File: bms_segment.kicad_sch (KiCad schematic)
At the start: 100 parts, among them J1 Conn_01x04, J2 Conn_01x04, J3 Conn_01x06, J4 Conn_01x13, SW1 SW_Push, U1 LMR516xx, U2 MAX14921, U3 ADuM1252, U4 STM32F103C8Tx, U5 MAX11163, U6 REF61xx

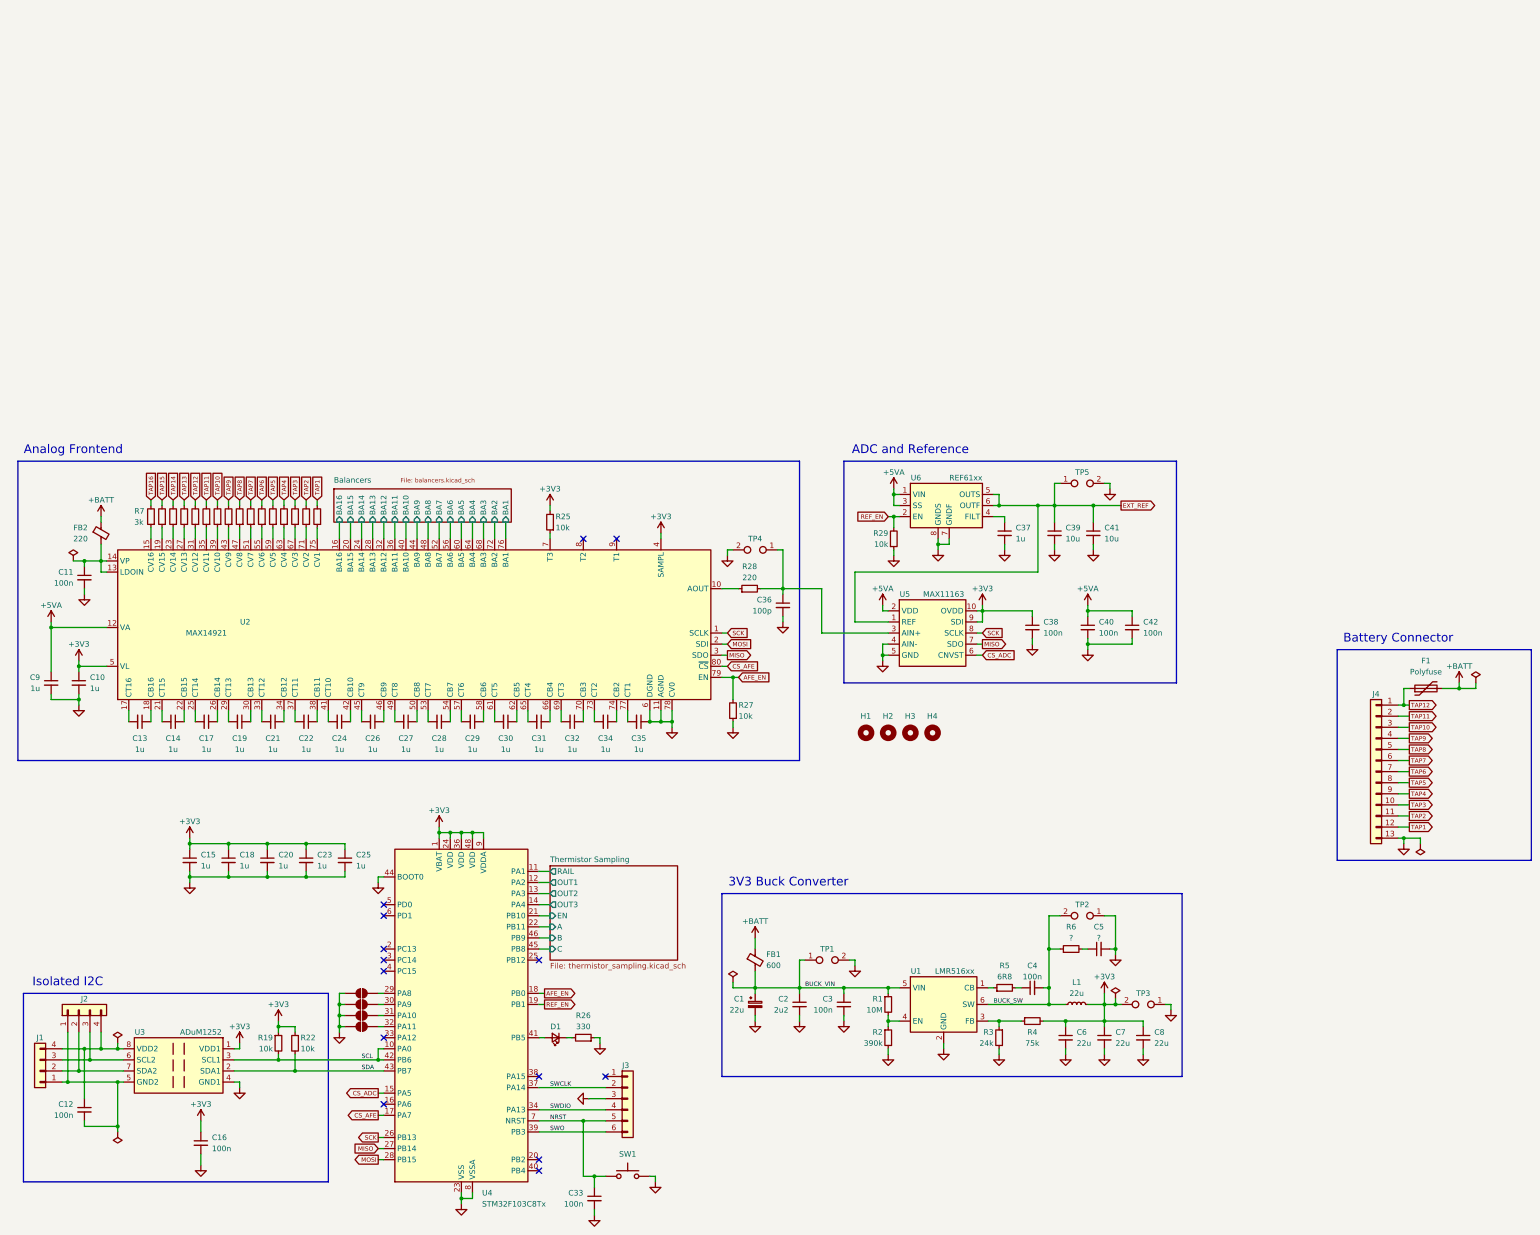
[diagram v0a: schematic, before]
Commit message: schematic: Add board interconnect connectors
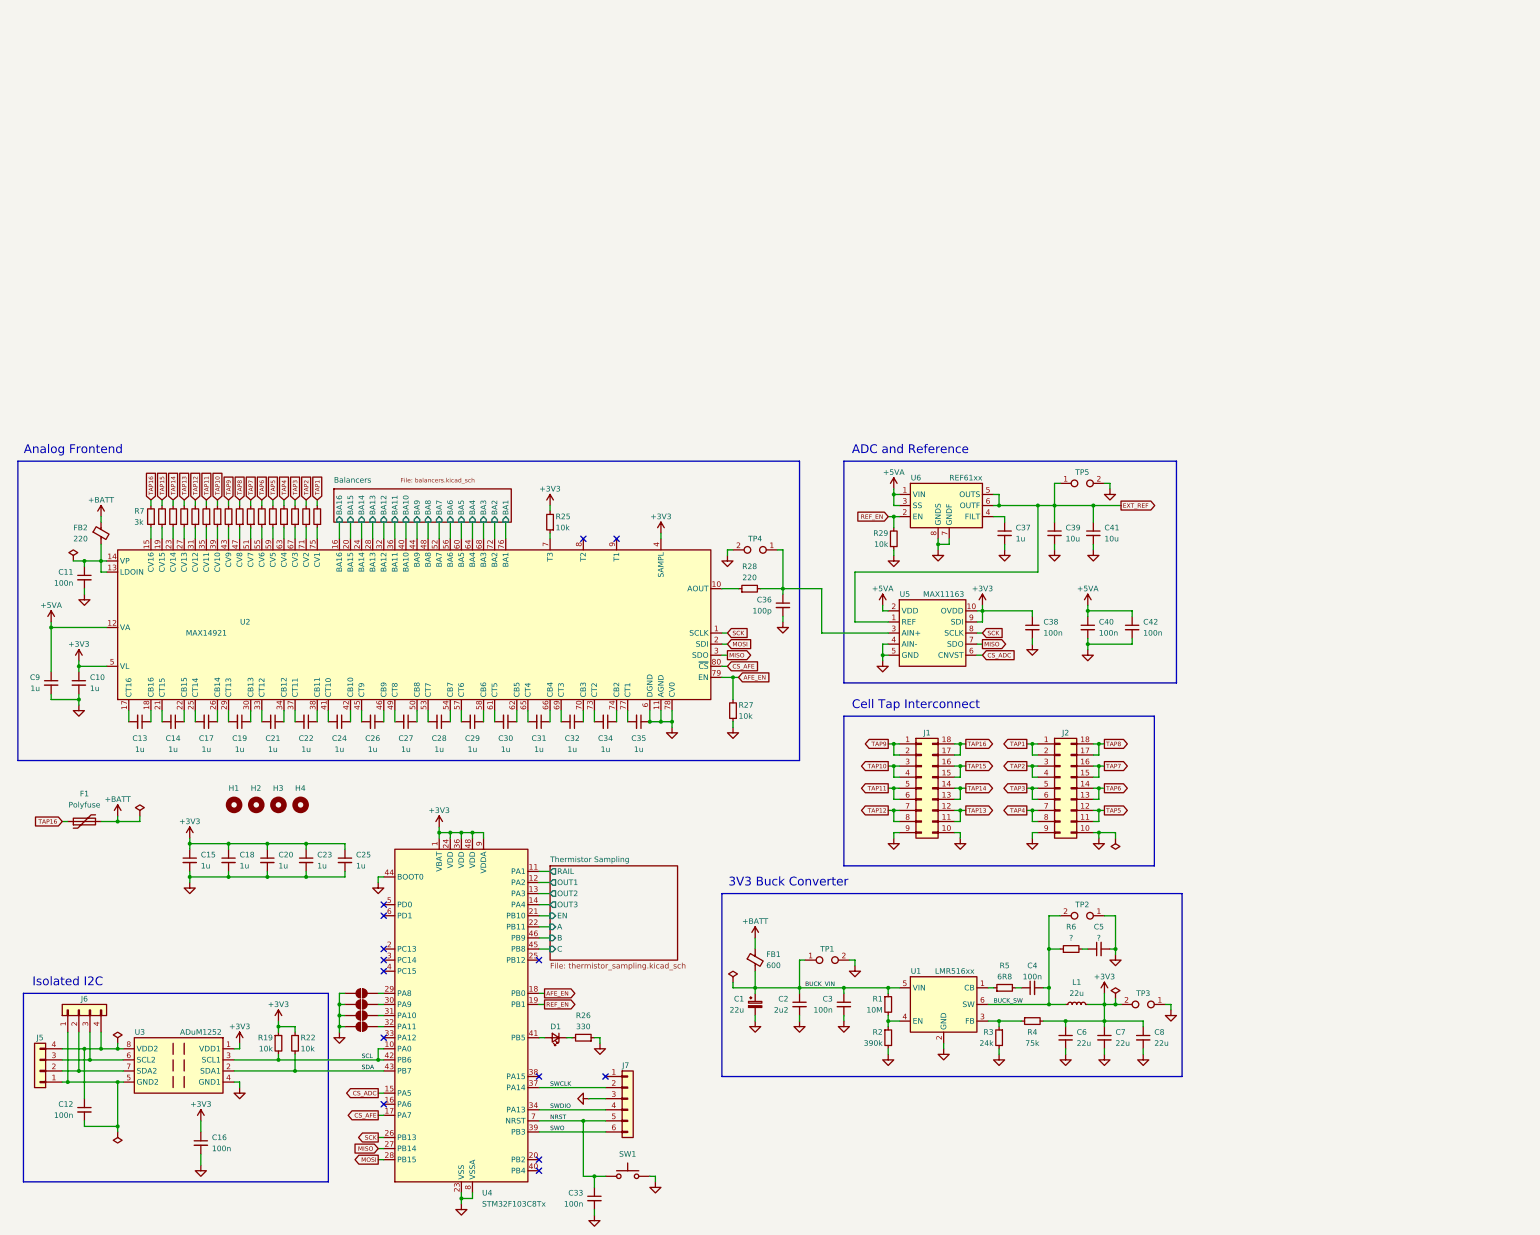
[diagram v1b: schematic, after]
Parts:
- removed J4: Conn_01x13, Connector_Phoenix_MC:PhoenixContact_MC_1,5_13-G-3.81_1x13_P3.81mm_Horizontal, symbol Connector_Generic:Conn_01x13
- added J1, J2: Conn_02x09_Counter_Clockwise, yfs:MolexMilliGrid2x9, symbol Connector_Generic:Conn_02x09_Counter_Clockwise
- renumbered J1 to J5, J2 to J6, J3 to J7
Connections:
- net GND: now also J1.10 (Pin_10), J1.9 (Pin_9), J2.10 (Pin_10), J2.9 (Pin_9)
- net TAP1: now also J2.1 (Pin_1), J2.2 (Pin_2)
- net TAP10: now also J1.3 (Pin_3), J1.4 (Pin_4)
- net TAP11: now also J1.5 (Pin_5), J1.6 (Pin_6)
- net TAP12: now also J1.7 (Pin_7), J1.8 (Pin_8); no longer F1.1
- net TAP13: now also J1.11 (Pin_11), J1.12 (Pin_12)
- net TAP14: now also J1.13 (Pin_13), J1.14 (Pin_14)
- net TAP15: now also J1.15 (Pin_15), J1.16 (Pin_16)
- net TAP16: now also F1.1, J1.17 (Pin_17), J1.18 (Pin_18)
- net TAP2: now also J2.3 (Pin_3), J2.4 (Pin_4)
- net TAP3: now also J2.5 (Pin_5), J2.6 (Pin_6)
- net TAP4: now also J2.7 (Pin_7), J2.8 (Pin_8)
- net TAP5: now also J2.11 (Pin_11), J2.12 (Pin_12)
- net TAP6: now also J2.13 (Pin_13), J2.14 (Pin_14)
- net TAP7: now also J2.15 (Pin_15), J2.16 (Pin_16)
- net TAP8: now also J2.17 (Pin_17), J2.18 (Pin_18)
- net TAP9: now also J1.1 (Pin_1), J1.2 (Pin_2)
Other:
- note added: "Cell Tap Interconnect"
- note removed: "Battery Connector"
- moved on the sheet: F1, H1, H2, H3, H4

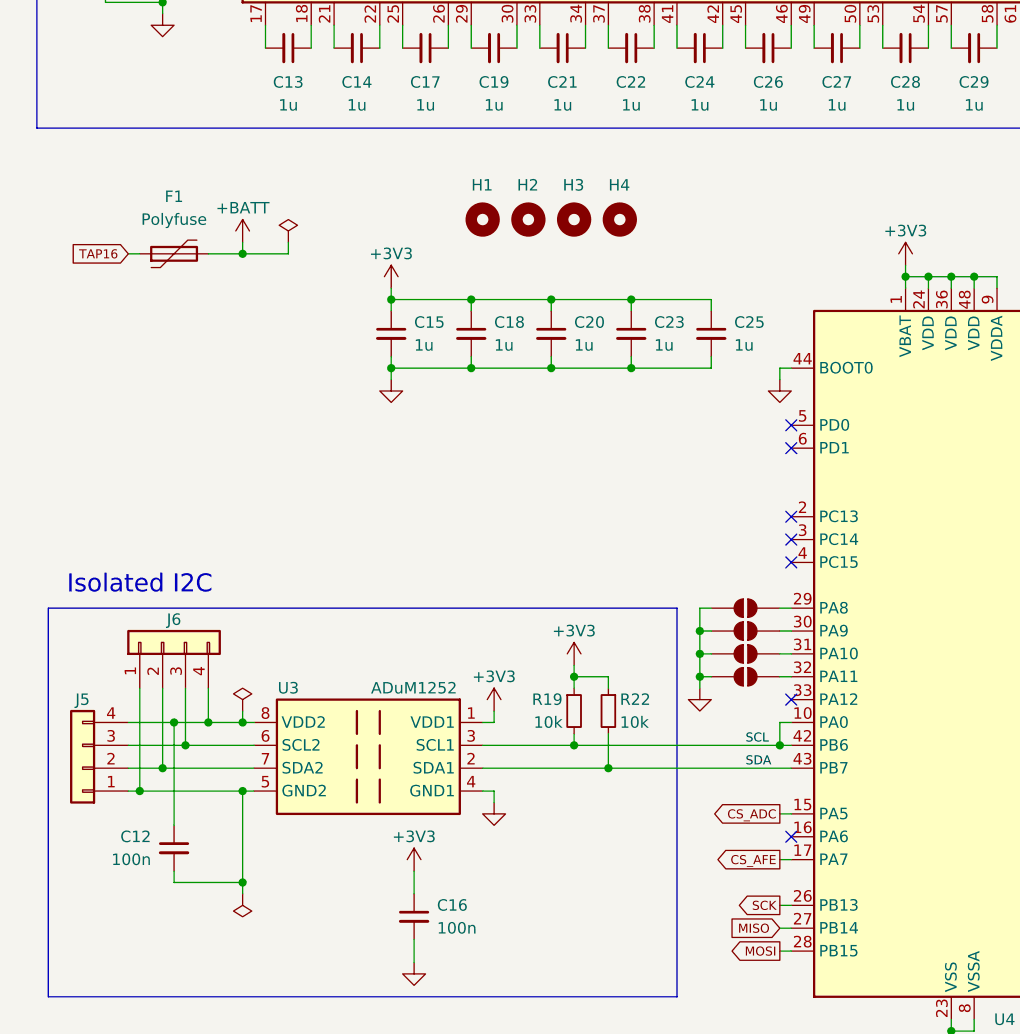
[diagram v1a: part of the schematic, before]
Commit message: schematic: Add external reference sampling by MCU
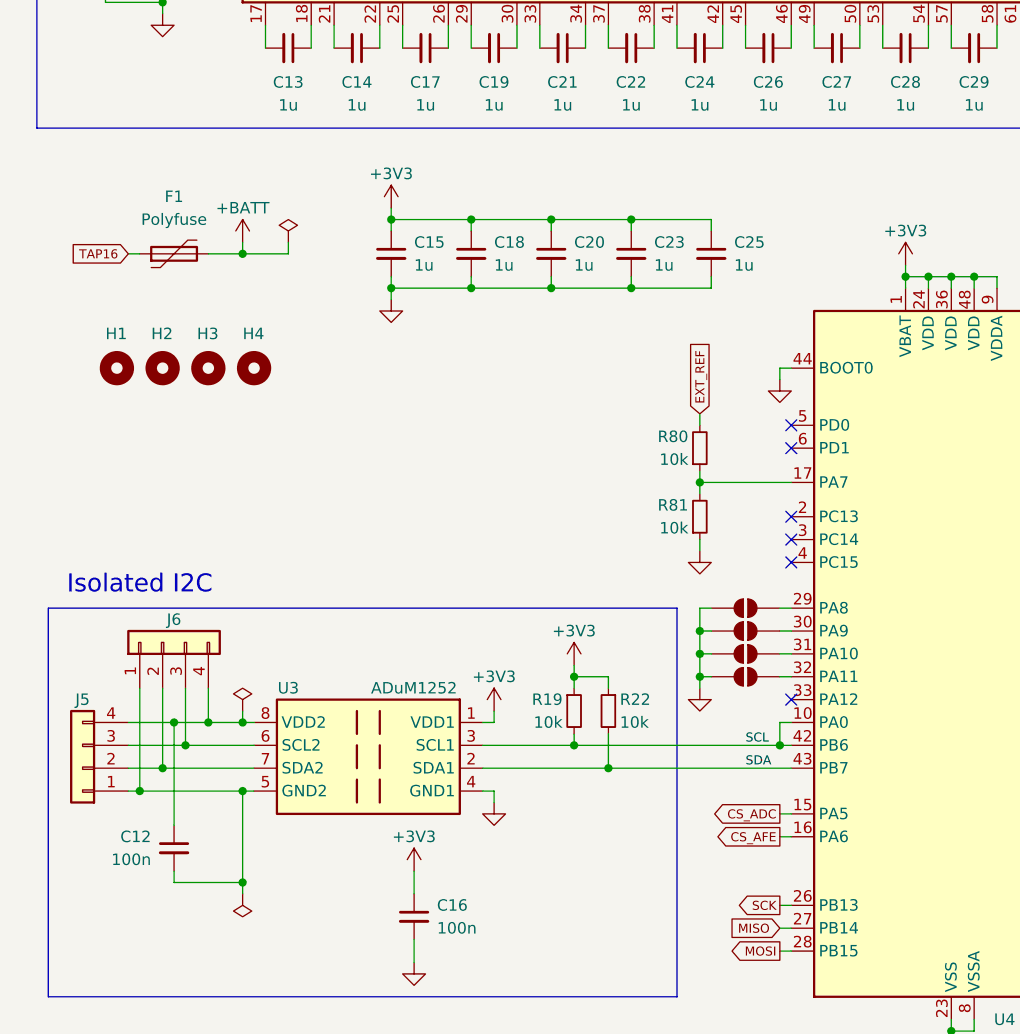
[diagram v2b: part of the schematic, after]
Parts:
- added R80, R81: 10k, Resistor_SMD:R_0603_1608Metric, symbol Device:R_Small
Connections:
- net CS_AFE: now also U4.16 (PA6); no longer U4.17 (PA7)
- net EXT_REF: now also R80.2
- net GND: now also R81.1
- new net: R80.1, R81.2, U4.17 (PA7)
- no-connect marks 14 -> 13
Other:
- moved on the sheet: C15, C18, C20, C23, C25, H1, H2, H3, H4
